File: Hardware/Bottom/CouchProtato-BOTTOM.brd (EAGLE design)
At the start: 33 x 33 mm, 32 parts, among them U1 AD5242-SO16

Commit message: Progress on routing bottom board and schematic
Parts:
- moved R20 34.7 mm to (29.5, 6.32), turned to 180 degrees
- moved C15 28.8 mm to (29.6, 4.48), turned to 0 degrees
- moved R21 28.2 mm to (32.0, 17.0), turned to 270 degrees
- moved R13 27.2 mm to (32.8, 6.41), turned to 270 degrees
- moved R23 27.0 mm to (29.6, 22.7), turned to 180 degrees
- moved R19 26.2 mm to (32.7, 9.73), turned to 270 degrees
- moved C19 24.7 mm to (29.5, 21.0), turned to 180 degrees
- moved R22 24.3 mm to (29.6, 19.2)
- moved C11 22.1 mm to (25.4, 7.85), turned to 90 degrees
- moved IMU1 22.1 mm to (6.44, 28.4), turned to 90 degrees
- moved C20 21.2 mm to (22.1, 6.94), turned to 270 degrees
- moved C14 21.0 mm to (29.8, 7.92), turned to 180 degrees
- moved R14 18.3 mm to (29.8, 9.60), turned to 0 degrees
- moved U1 17.9 mm to (10.9, 10.2)
- moved R17 17.0 mm to (25.1, 19.7), turned to 90 degrees
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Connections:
- removed net LED: Q1.3
- net 3.3V: now also J1.4
- net GND: now also J1.3
- net LED.C: now also Q1.3
- net SCL: now also J1.2
- net SDA: now also J1.1
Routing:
- net A6/TIA: track 0.00 -> 34.3 mm, vias 0 -> 2
- net PD.C: track 0.00 -> 25.0 mm, vias 0 -> 2
- net N$19: track 0.00 -> 22.2 mm
- net GND: track 0.00 -> 19.4 mm, vias 0 -> 8
- net G.W2: track 0.00 -> 17.6 mm, vias 0 -> 2
- net A7/PPG: track 0.00 -> 16.2 mm
- net N$17: track 0.00 -> 10.0 mm, vias 0 -> 2
- net N$18: track 0.00 -> 5.86 mm
- net N$15: track 0.00 -> 5.78 mm
- net N$13: track 0.00 -> 5.39 mm
- net N$16: track 0.00 -> 4.12 mm
- net N$10: track 0.00 -> 3.27 mm
- net SDA: track 0.00 -> 2.17 mm
- net SCL: track 0.00 -> 2.17 mm
- net N$20: track 0.00 -> 1.59 mm
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- added copper zone on layer 16, net GND

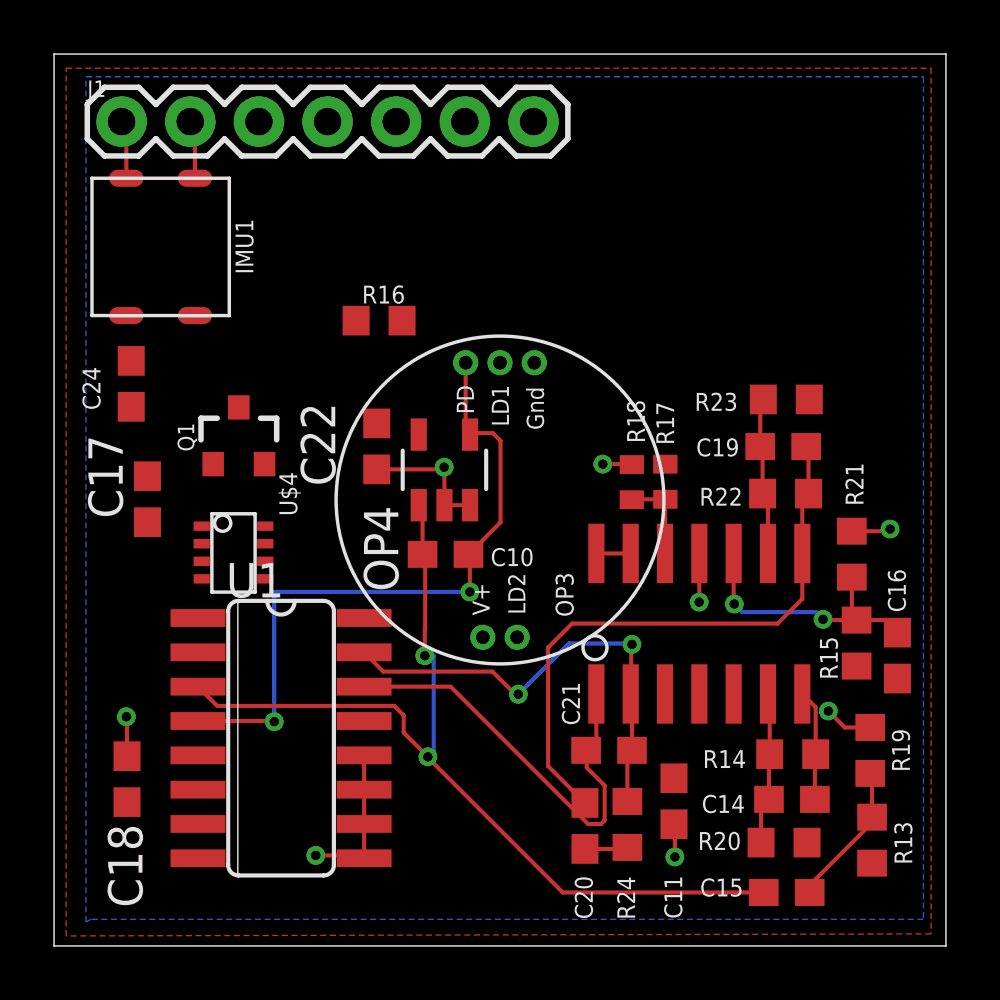
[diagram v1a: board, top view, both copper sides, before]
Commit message: finished routing bottom board and began top. finished take 003.
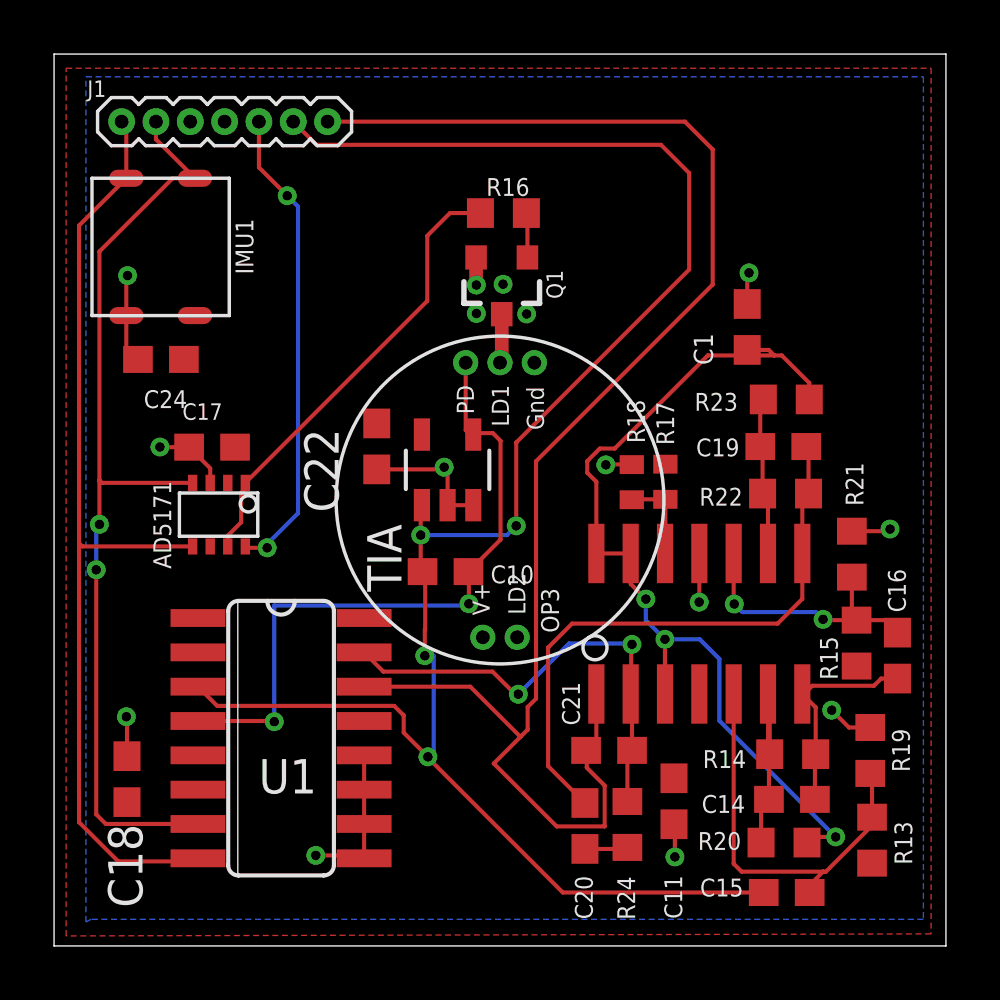
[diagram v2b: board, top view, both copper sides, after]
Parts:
- removed OP4: (no value), LinnesLab-AnalogIC:SOT23-5
- removed U$4: AD5171, LinnesLab-DigitalIC:SOT-23-8
- added AD5171: AD5171, LinnesLab-DigitalIC:SOT-23-8
- added C1: 100n, LinnesLab-Passives:C0603
- added TIA: (no value), LinnesLab-AnalogIC:SOT23-5
- J1: device LinnesLab-Connectors:1X07 -> LinnesLab-Connectors:1X07_1.27MM
- moved Q1 11.2 mm to (19.1, 27.0), turned to 180 degrees
- moved R16 6.08 mm to (19.1, 29.6)
- moved C17 3.07 mm to (8.35, 21.0), turned to 0 degrees
- moved C24 1.42 mm to (6.45, 24.2), turned to 0 degrees
- moved C10 0.64 mm to (17.0, 16.3)
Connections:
- net 3.3V: now also AD5171.2, AD5171.6, TIA.5; no longer OP4.5, U$4.2, U$4.6
- net A6/TIA: now also J1.6, TIA.1; no longer J1.5, OP4.1
- net D29/LED.CTRL: now also AD5171.8, J1.5; no longer J1.6, U$4.8
- net GND: now also AD5171.3, C1.2, TIA.2, TIA.3; no longer OP4.2, OP4.3, U$4.3
- net N$9: now also AD5171.1, AD5171.7; no longer U$4.1, U$4.7
- net PD.C: now also TIA.4; no longer OP4.4
- net SCL: now also AD5171.4; no longer U$4.4
- net SDA: now also AD5171.5; no longer U$4.5
- net VREF: now also C1.1
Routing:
- net A7/PPG: track 16.2 -> 57.7 mm
- net A6/TIA: track 34.3 -> 69.1 mm, vias 2 -> 4
- net SDA: track 2.17 -> 36.0 mm
- net SCL: track 2.17 -> 35.6 mm, vias 0 -> 2
- net VREF: track 1.27 -> 34.3 mm, vias 0 -> 3
- net D29/LED.CTRL: track 0.00 -> 17.7 mm, vias 0 -> 2
- net N$9: track 0.00 -> 16.9 mm
- net N$13: track 5.39 -> 15.2 mm
- net GND: track 19.4 -> 27.8 mm, vias 8 -> 15
- net N$16: track 4.12 -> 7.85 mm
- net N$15: track 5.78 -> 7.92 mm
- net LED.C: track 0.00 -> 1.82 mm
- net N$8: track 0.00 -> 1.66 mm

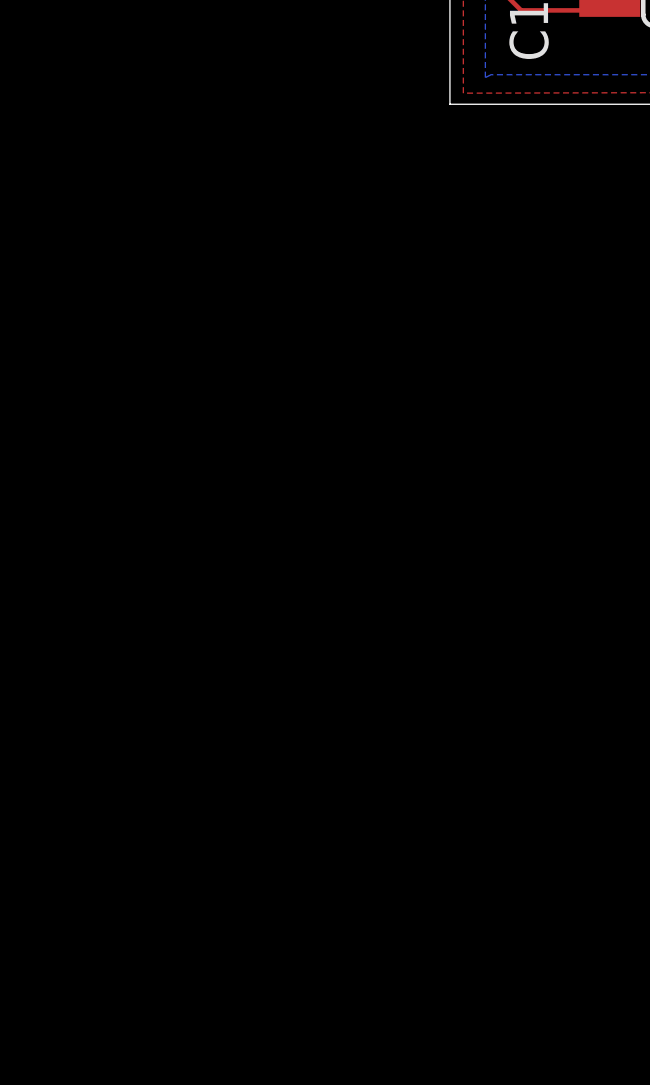
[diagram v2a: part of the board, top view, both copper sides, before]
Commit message: Finished take 7, one more how to video to go, reorganizing and finalizing boards
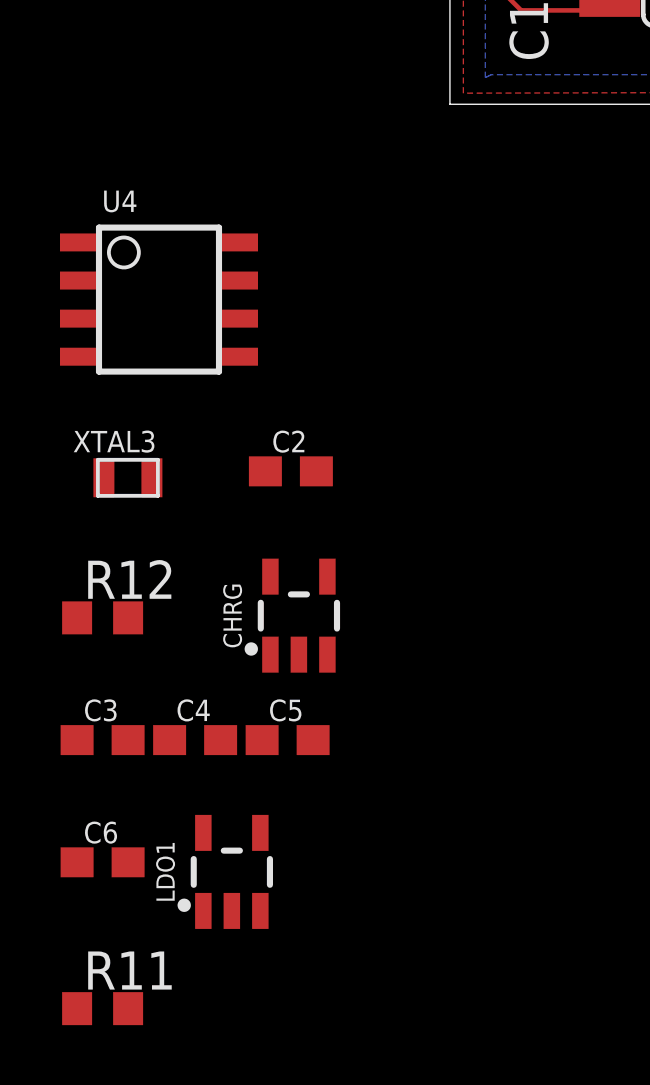
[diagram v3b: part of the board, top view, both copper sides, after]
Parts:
- added C2, C5, C6: 1u, LinnesLab-Passives:C0603
- added C3, C4: 4.7u, LinnesLab-Passives:C0603
- added CHRG: MCP73831, LinnesLab-Power:SOT23-5
- added LDO1: MIC5504, LinnesLab-Power:SOT23-5
- added R11: (no value), LinnesLab-Passives:R0603
- added R12: 100k, LinnesLab-Passives:R0603
- added U4: PCF8523, LinnesLab-Clocks:SO8
- added XTAL3: 32.7680kHz, LinnesLab-Clocks:2-SMD.NOLEAD.2.0MMTO1.2MM
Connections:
- new net D27/CHRG.STATUS: CHRG.1, R12.1
- new net N$1: U4.2, XTAL3.P$1
- new net N$2: U4.1, XTAL3.P$2
- new net N$3: CHRG.5, R11.2
- new net VBAT: U4.3
- new net VIN1: C4.2, C5.2, CHRG.4, LDO1.1, LDO1.3, R12.2
- new net VLIPO: C3.1, CHRG.3
- net 3.3V: now also C2.1, C6.1, LDO1.5, U4.8
- net GND: now also C2.2, C3.2, C4.1, C5.1, C6.2, CHRG.2, LDO1.2, R11.1, U4.4
- net SCL: now also U4.6
- net SDA: now also U4.5

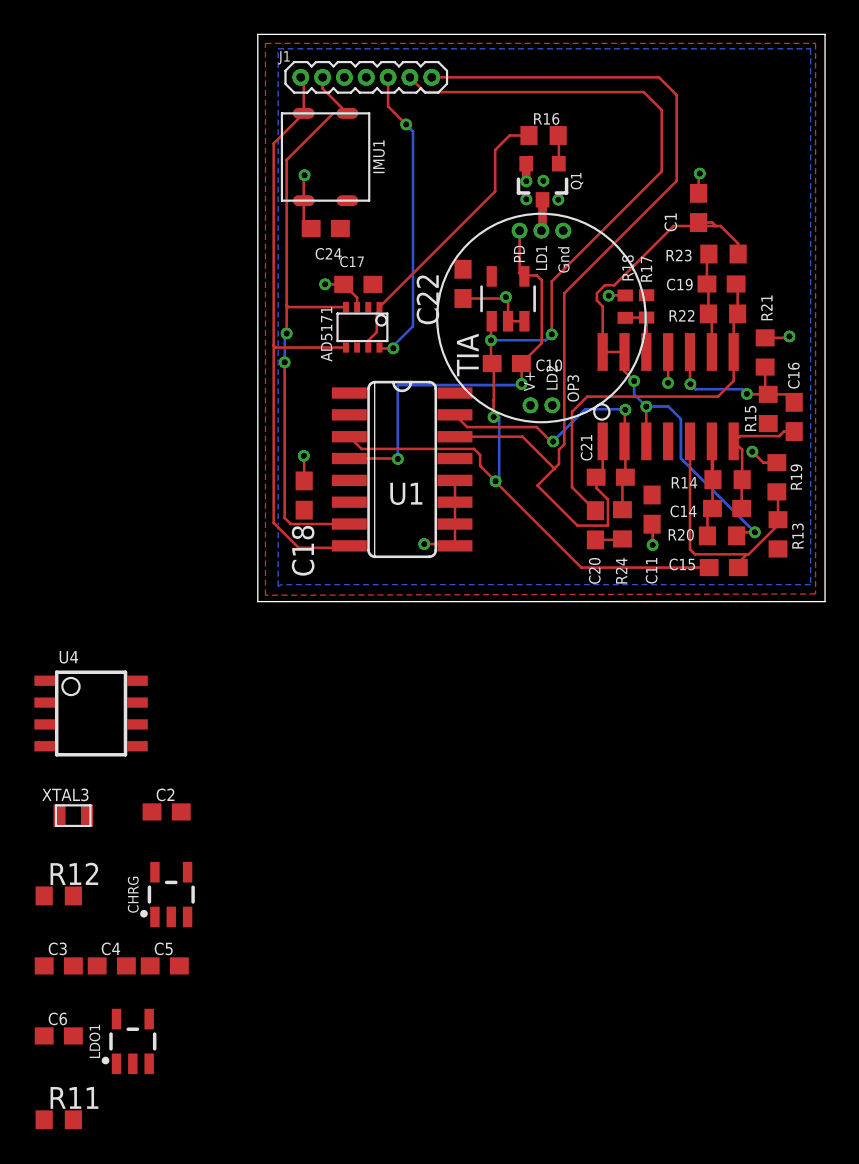
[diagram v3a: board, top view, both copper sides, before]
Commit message: Finished first revisions of EAGLE designs for smartwatch
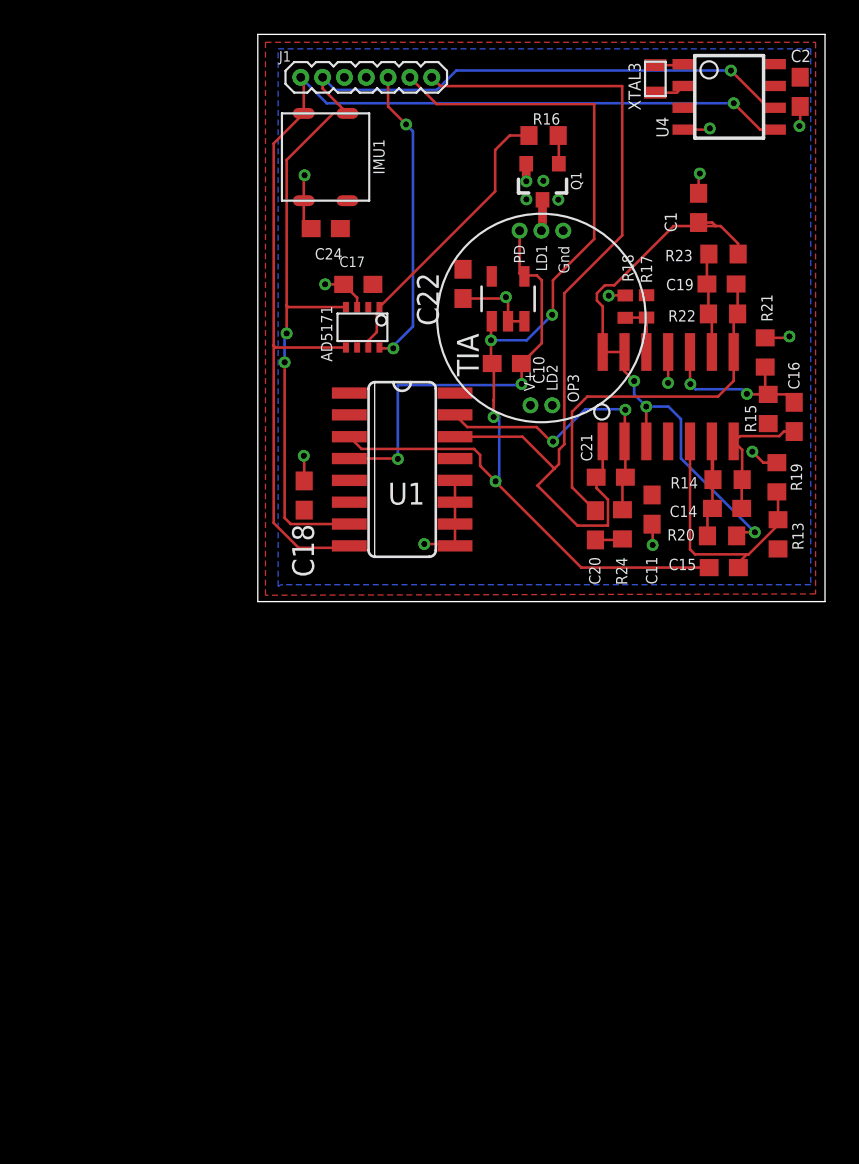
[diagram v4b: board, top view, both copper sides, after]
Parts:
- removed C3, C4: 4.7u, LinnesLab-Passives:C0603
- removed C5, C6: 1u, LinnesLab-Passives:C0603
- removed CHRG: MCP73831, LinnesLab-Power:SOT23-5
- removed LDO1: MIC5504, LinnesLab-Power:SOT23-5
- removed R11: (no value), LinnesLab-Passives:R0603
- removed R12: 100k, LinnesLab-Passives:R0603
- moved C2 55.8 mm to (34.1, 32.2), turned to 270 degrees
- moved XTAL3 54.6 mm to (25.6, 32.9), turned to 90 degrees
- moved U4 51.6 mm to (29.9, 31.9)
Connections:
- net A6/TIA renamed A5/TIA
- net A7/PPG renamed A4/PPG
- net D29/LED.CTRL renamed D30/LED.CTRL
- removed net D27/CHRG.STATUS: CHRG.1, R12.1
- removed net N$3: CHRG.5, R11.2
- removed net VIN1: C4.2, C5.2, CHRG.4, LDO1.1, LDO1.3, R12.2
- removed net VLIPO: C3.1, CHRG.3
- net 3.3V: no longer C6.1, LDO1.5
- net GND: no longer C3.2, C4.1, C5.1, C6.2, CHRG.2, LDO1.2, R11.1
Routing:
- net SDA: track 36.0 -> 64.9 mm, vias 0 -> 1
- net SCL: track 35.6 -> 63.6 mm, vias 2 -> 3
- net A5/TIA: track 69.1 -> 63.2 mm
- net A4/PPG: track 57.7 -> 53.6 mm
- net GND: track 27.8 -> 30.5 mm, vias 15 -> 17
- net N$1: track 0.00 -> 1.81 mm
- net N$2: track 0.00 -> 1.67 mm
